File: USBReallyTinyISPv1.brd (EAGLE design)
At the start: 27.9 x 16.5 mm, 20 parts, among them IC1 ATTINY2313, IC2 74AC125D, Q1 12 MHz, X1 miniUSB-B

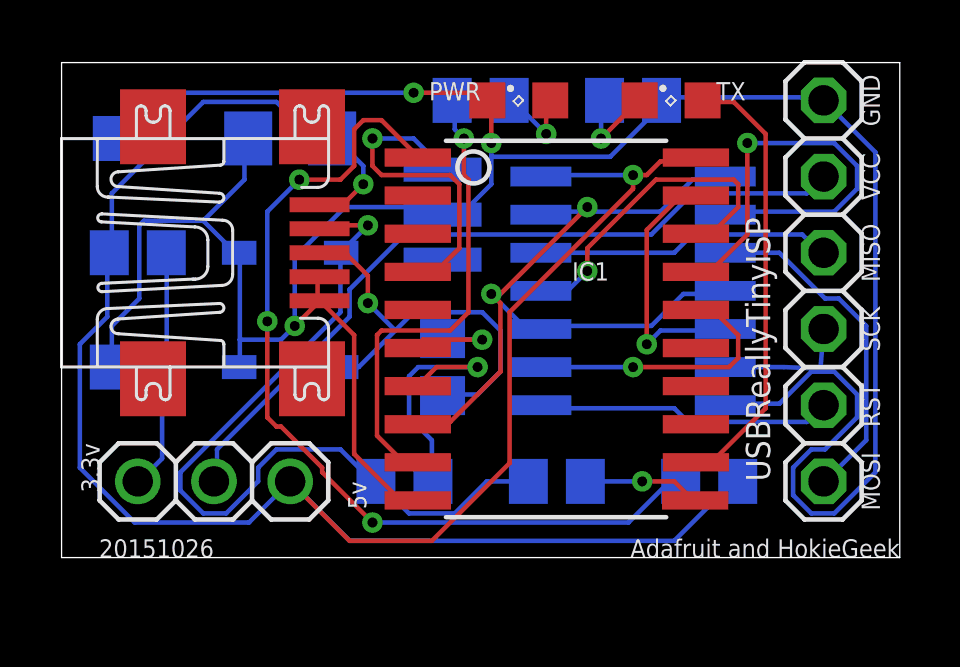
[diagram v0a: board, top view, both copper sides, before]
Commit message: Because it was just too big
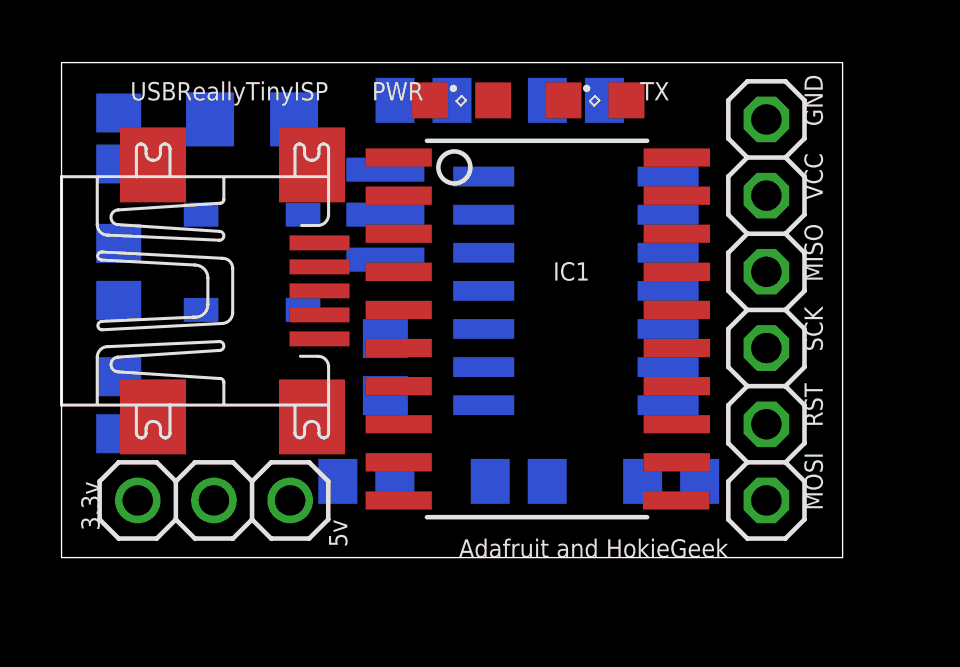
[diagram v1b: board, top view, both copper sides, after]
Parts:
- moved LED1 2.54 mm to (17.8, 16.5)
- moved D2 2.29 mm to (6.35, 9.53)
- moved JP2 2.01 mm to (23.5, 9.53)
- moved IC2 1.91 mm to (17.1, 10.2)
- moved R1 1.91 mm to (17.1, 16.5)
- moved R2 1.91 mm to (12.1, 16.5)
- moved LED2 1.90 mm to (13.3, 16.5)
- moved Q1 1.90 mm to (10.8, 12.7)
- moved R3 1.90 mm to (10.8, 7.62)
- moved D1 1.80 mm to (6.35, 12.7)
- moved C2 1.42 mm to (6.35, 15.9)
- moved R8 1.42 mm to (1.91, 6.35), turned to 90 degrees
- moved R5 1.27 mm to (15.2, 3.81), turned to 0 degrees
- moved R4 1.27 mm to (10.2, 3.81)
- moved R6 1.27 mm to (20.3, 3.81), turned to 0 degrees
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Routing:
- net GND: track 93.6 -> 0.00 mm, vias 3 -> 0
- net VCC: track 73.5 -> 0.00 mm, vias 2 -> 0
- net N$4: track 30.3 -> 0.00 mm, vias 3 -> 0
- net N$11: track 27.5 -> 0.00 mm, vias 1 -> 0
- net N$12: track 26.3 -> 0.00 mm, vias 2 -> 0
- net N$13: track 25.7 -> 0.00 mm
- net N$5: track 15.7 -> 0.00 mm, vias 1 -> 0
- net N$1: track 14.8 -> 0.00 mm
- net MOSI': track 14.8 -> 0.00 mm, vias 1 -> 0
- net N$10: track 14.1 -> 0.00 mm, vias 1 -> 0
- net MOSI: track 11.5 -> 0.00 mm
- net MISO': track 11.2 -> 0.00 mm, vias 1 -> 0
- net N$2: track 10.7 -> 0.00 mm, vias 1 -> 0
- net MISO: track 9.93 -> 0.00 mm
- net RST: track 9.92 -> 0.00 mm
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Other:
- board size 27.9 x 16.5 mm -> 26 x 16.5 mm
- board text added: "20151027"
- board text removed: "20151026"

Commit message: Lots of tweaks to get a tiny little board!
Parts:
- moved R1 2.29 mm to (19.1, 15.2), turned to 180 degrees
- moved R2 2.29 mm to (14.0, 15.2)
- moved R5 1.91 mm to (15.2, 1.91)
- moved R6 1.91 mm to (20.3, 1.91)
- moved IC2 1.90 mm to (17.1, 8.26)
- moved LED1 1.80 mm to (19.1, 15.2), turned to 180 degrees
- moved IC1 1.80 mm to (17.1, 7.62)
- moved LED2 1.42 mm to (14.0, 15.2)
- moved R3 1.42 mm to (10.2, 6.35)
- moved JP2 1.42 mm to (24.1, 8.26)
- moved R4 1.27 mm to (10.2, 2.54)
- moved JP1 1.27 mm to (5.08, 1.91)
- moved C1 1.27 mm to (1.91, 14.0)
- moved C2 1.27 mm to (6.35, 14.6)
- moved D1 1.27 mm to (6.35, 11.4)
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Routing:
- net VCC: track 0.00 -> 93.8 mm, vias 0 -> 2
- net GND: track 0.00 -> 90.6 mm, vias 0 -> 4
- net N$5: track 0.00 -> 39.3 mm, vias 0 -> 1
- net N$11: track 0.00 -> 28.0 mm, vias 0 -> 2
- net N$13: track 0.00 -> 26.0 mm
- net N$12: track 0.00 -> 25.4 mm, vias 0 -> 3
- net N$4: track 0.00 -> 17.7 mm, vias 0 -> 1
- net N$10: track 0.00 -> 16.9 mm, vias 0 -> 1
- net N$1: track 0.00 -> 16.0 mm
- net MOSI: track 0.00 -> 14.8 mm
- net MISO': track 0.00 -> 11.1 mm, vias 0 -> 3
- net SCK': track 0.00 -> 11.0 mm, vias 0 -> 1
- net MISO: track 0.00 -> 10.7 mm
- net RST: track 0.00 -> 10.6 mm
- net N$3: track 0.00 -> 10.3 mm, vias 0 -> 1
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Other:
- board size 26 x 16.5 mm -> 26.7 x 16.5 mm
- board text removed: "0.1uF"
- board text removed: "1.5k"
- board text removed: "100uF"
- board text removed: "10k"
- board text removed: "12Mhz"
- board text removed: "3.6v"
- board text removed: "47"
- board text removed: "47k"
- board text removed: "91k"

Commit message: Tweak Tweak!
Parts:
- moved JP2 0.64 mm to (24.8, 8.26)
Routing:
- net VCC: track 93.8 -> 63.2 mm
- net N$5: track 39.3 -> 16.8 mm
- net N$4: track 17.7 -> 38.8 mm, vias 1 -> 3
- net N$12: track 25.4 -> 35.5 mm
- net SCK': track 11.0 -> 15.6 mm
- net N$11: track 28.0 -> 23.7 mm, vias 2 -> 3
- net MOSI: track 14.8 -> 12.4 mm
- net N$10: track 16.9 -> 18.8 mm, vias 1 -> 2
- net N$1: track 16.0 -> 14.6 mm
- net N$3: track 10.3 -> 9.05 mm
- net N$6: track 3.64 -> 2.37 mm
- net GND: track 90.6 -> 91.4 mm, vias 4 -> 2
- net RST: track 10.6 -> 11.2 mm
- net SCK: track 4.48 -> 5.10 mm
- net N$13: track 26.0 -> 26.6 mm, vias 0 -> 1
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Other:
- board size 26.7 x 16.5 mm -> 27.3 x 16.5 mm

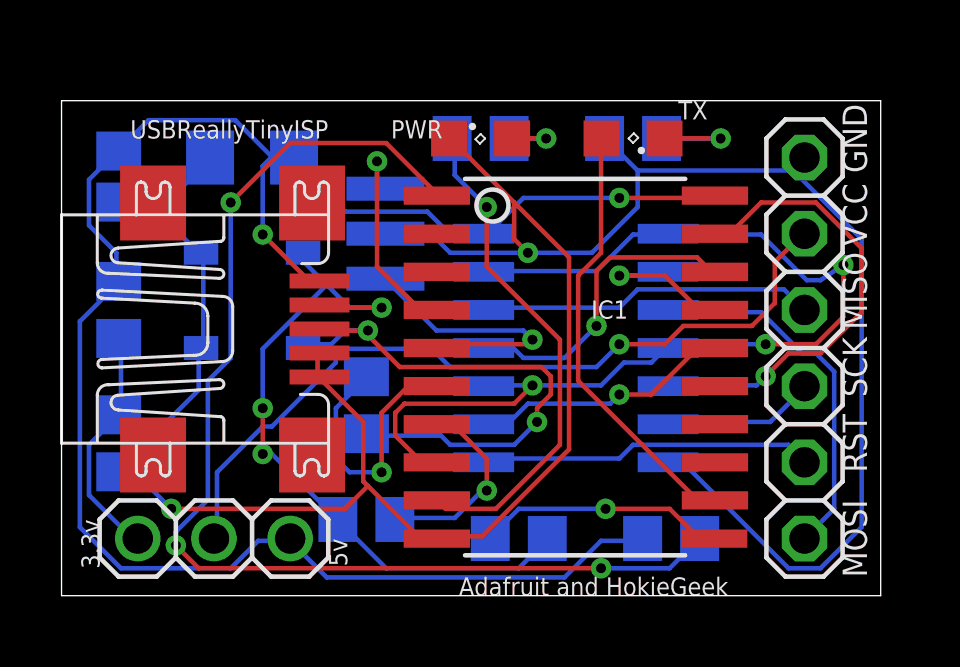
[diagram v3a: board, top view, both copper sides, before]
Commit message: Changed size of 1.5kOhm resistors
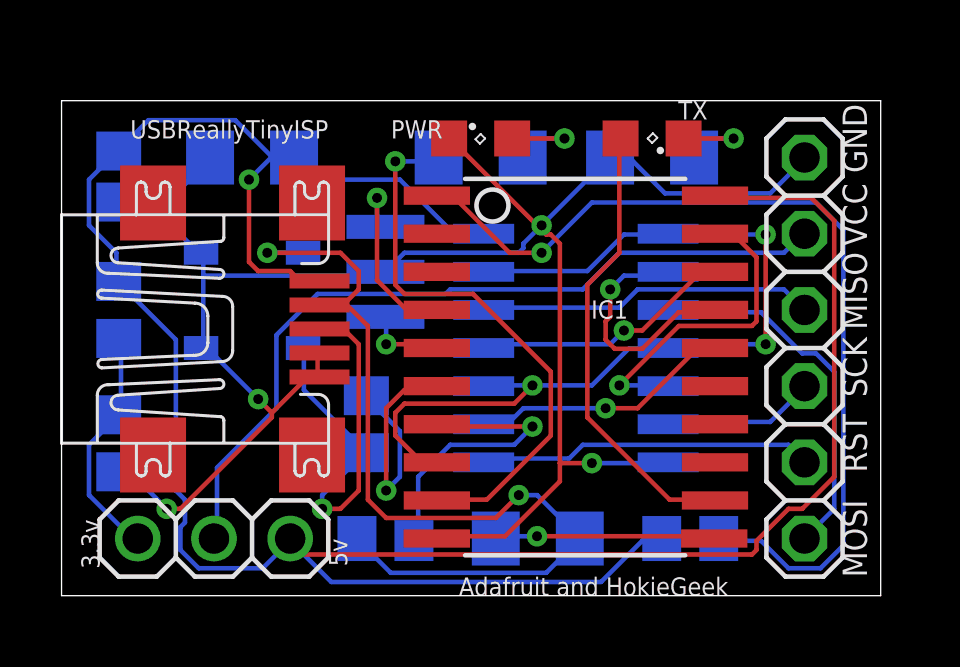
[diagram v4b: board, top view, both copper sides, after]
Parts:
- R1, R2, R5: value 1.5K -> 1.5k; device resistor:R0805 -> SparkFun-Resistors:1206
- moved Q1 1.27 mm to (10.8, 10.8)
- moved R4 0.90 mm to (10.8, 1.91)
- moved R1 0.90 mm to (19.7, 14.6)
- moved R2 0.63 mm to (14.0, 14.6)
- moved R3 0.63 mm to (10.2, 5.71)
- moved R5 0.63 mm to (15.9, 1.91)
- moved LED1 0.63 mm to (19.7, 15.2)
- moved R6 0.63 mm to (21.0, 1.91)
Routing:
- net GND: track 91.4 -> 67.0 mm, vias 2 -> 4
- net VCC: track 63.2 -> 87.0 mm, vias 2 -> 1
- net N$4: track 38.8 -> 30.8 mm, vias 3 -> 1
- net N$11: track 23.7 -> 31.0 mm, vias 3 -> 2
- net N$3: track 9.05 -> 2.72 mm
- net SCK': track 15.6 -> 10.9 mm
- net N$12: track 35.5 -> 31.1 mm
- net N$10: track 18.8 -> 14.7 mm, vias 2 -> 1
- net N$9: track 6.67 -> 9.85 mm
- net MOSI': track 5.34 -> 8.22 mm
- net N$5: track 16.8 -> 18.8 mm
- net MISO': track 10.5 -> 8.77 mm
- net N$6: track 2.37 -> 3.40 mm
- net N$14: track 8.29 -> 7.38 mm
- net N$2: track 7.15 -> 6.29 mm
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
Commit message: Updated headers to have bigger pads
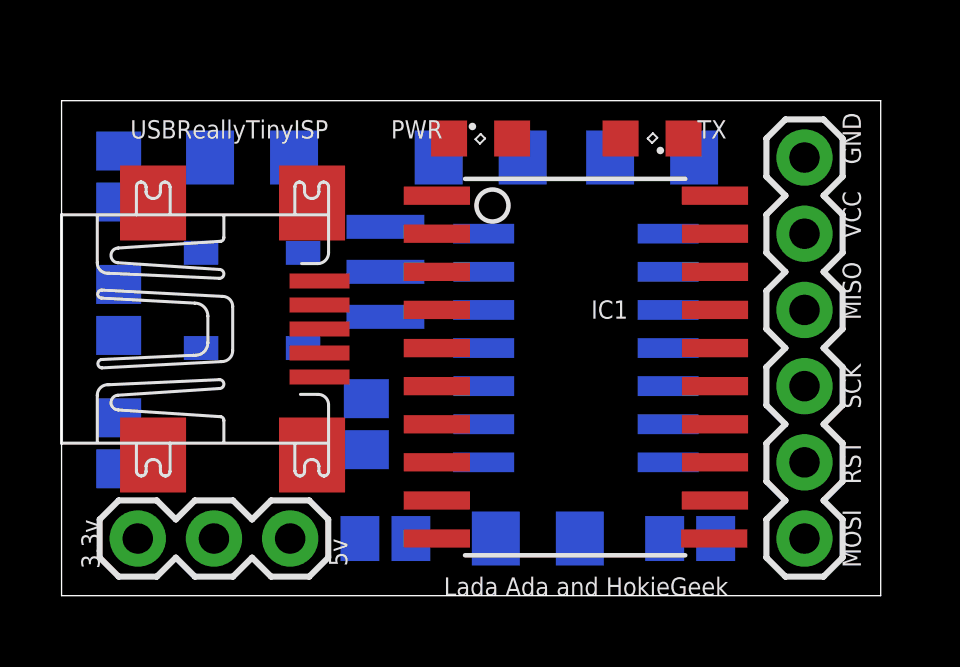
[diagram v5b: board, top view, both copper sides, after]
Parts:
- JP1: device adafruit:1X03 -> SparkFun-Connectors:1X06
- JP2: device adafruit:1X06 -> mine:1X03
- moved JP2 23.1 mm to (2.54, 1.91), turned to 0 degrees
- moved JP1 19.7 mm to (24.8, 1.91), turned to 90 degrees
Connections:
- net GND: now also JP1.1; no longer JP2.1
- net MISO: now also JP1.3; no longer JP2.3
- net MOSI: now also JP1.6; no longer JP2.6
- net N$15: now also JP2.1; no longer JP1.1
- net RST: now also JP1.5; no longer JP2.5
- net SCK: now also JP1.4; no longer JP2.4
- net VCC: now also JP2.3; no longer JP1.3
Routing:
- net VCC: track 87.0 -> 0.00 mm, vias 1 -> 0
- net GND: track 67.0 -> 0.00 mm, vias 4 -> 0
- net N$12: track 31.1 -> 0.00 mm, vias 3 -> 0
- net N$11: track 31.0 -> 0.00 mm, vias 2 -> 0
- net N$4: track 30.8 -> 0.00 mm, vias 1 -> 0
- net N$13: track 26.6 -> 0.00 mm
- net N$5: track 18.8 -> 0.00 mm, vias 1 -> 0
- net N$1: track 15.2 -> 0.00 mm
- net N$10: track 14.7 -> 0.00 mm, vias 1 -> 0
- net MOSI: track 12.4 -> 0.00 mm
- net MISO: track 11.3 -> 0.00 mm
- net RST: track 11.2 -> 0.00 mm
- net SCK': track 10.9 -> 0.00 mm, vias 1 -> 0
- net N$9: track 9.85 -> 0.00 mm, vias 1 -> 0
- net MISO': track 8.77 -> 0.00 mm, vias 1 -> 0
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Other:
- board text added: "Lada Ada and HokieGeek"
- board text removed: "Adafruit and HokieGeek"

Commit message: Rerouted based on some updates
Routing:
- net GND: track 0.00 -> 96.3 mm, vias 0 -> 3
- net VCC: track 0.00 -> 71.7 mm, vias 0 -> 3
- net N$11: track 0.00 -> 26.8 mm, vias 0 -> 1
- net N$12: track 0.00 -> 23.2 mm, vias 0 -> 2
- net N$4: track 0.00 -> 23.1 mm, vias 0 -> 1
- net N$13: track 0.00 -> 23.1 mm
- net RST: track 0.00 -> 19.7 mm
- net MISO: track 0.00 -> 17.0 mm
- net N$5: track 0.00 -> 16.7 mm, vias 0 -> 1
- net N$10: track 0.00 -> 16.1 mm, vias 0 -> 1
- net N$1: track 0.00 -> 15.4 mm
- net SCK': track 0.00 -> 10.6 mm, vias 0 -> 1
- net N$9: track 0.00 -> 9.57 mm, vias 0 -> 1
- net MISO': track 0.00 -> 9.50 mm, vias 0 -> 1
- net RST': track 0.00 -> 8.75 mm, vias 0 -> 1
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
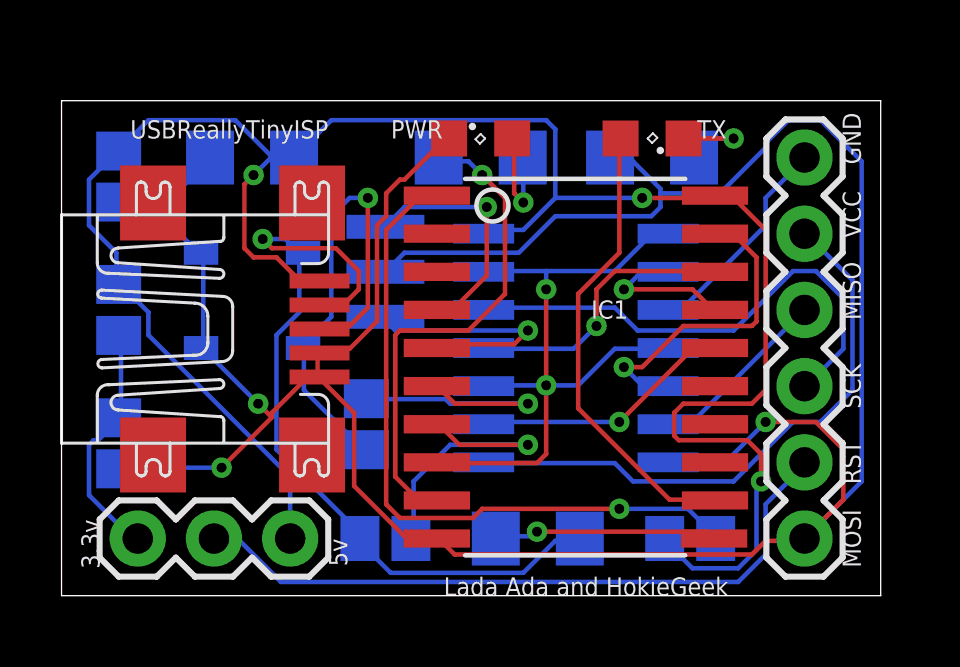
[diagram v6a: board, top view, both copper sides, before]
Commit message: Working on the schematic as I start to find flaws in my design
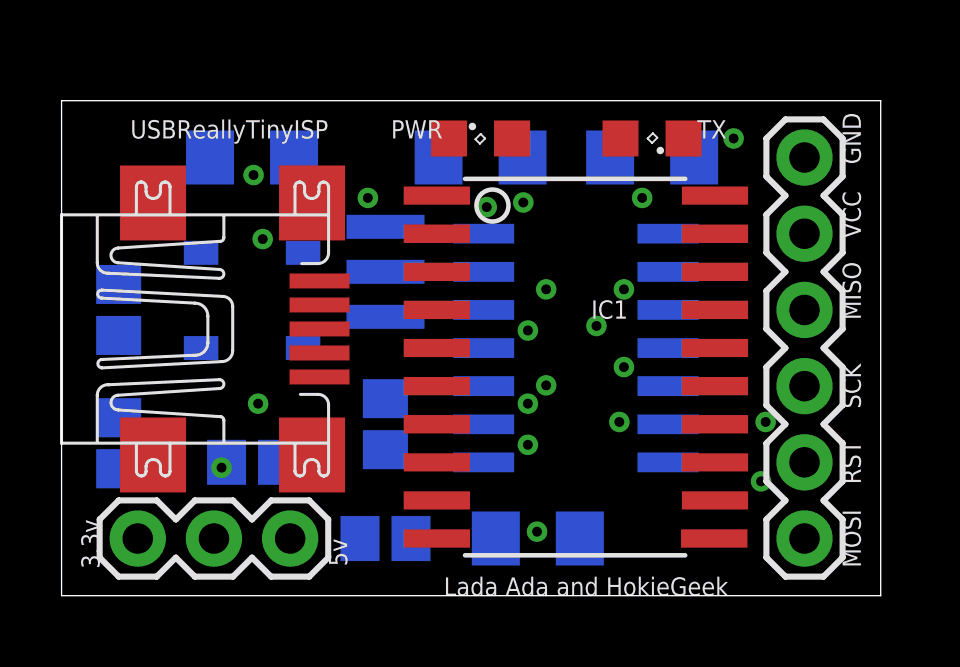
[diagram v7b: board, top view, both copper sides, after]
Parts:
- removed R6: 10K, resistor:R0805
- R7: value 47K -> 1.5k
- R8: value 91K -> 3k
- moved C1 12.1 mm to (10.8, 5.71)
- moved R3 4.02 mm to (6.35, 4.45), turned to 0 degrees
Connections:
- net N$12 renamed BEN
- net N$13 renamed VPWR
- removed net N$4 (its old number): IC1.1, R6.1
- net RST: no longer IC2.8
- net VCC: no longer R6.2
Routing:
- net GND: track 96.3 -> 0.00 mm
- net VCC: track 71.7 -> 0.00 mm
- net N$11: track 26.8 -> 0.00 mm
- net BEN: track 23.2 -> 0.00 mm
- net N$4 (its old number): track 23.1 -> 0.00 mm, vias 1 -> 0
- net VPWR: track 23.1 -> 0.00 mm
- net RST: track 19.7 -> 0.00 mm
- net MISO: track 17.0 -> 0.00 mm
- net N$4: track 16.7 -> 0.00 mm, vias 1 -> 0
- net N$10: track 16.1 -> 0.00 mm
- net N$1: track 15.4 -> 0.00 mm
- net SCK': track 10.6 -> 0.00 mm
- net N$9: track 9.57 -> 0.00 mm
- net MISO': track 9.50 -> 0.00 mm
- net RST': track 8.75 -> 0.00 mm
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
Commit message: Finally removed that freaking border
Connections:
- net RST: now also IC2.8
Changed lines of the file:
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@@
 <signal name="RST">
 <contactref element="JP1" pad="5"/>
+<contactref element="IC2" pad="8"/>
+<wire x1="14.0716" y1="4.445" x2="24.765" y2="12.065" width="0" layer="19" extent="16-16"/>
 </signal>
 <signal name="N$14">
